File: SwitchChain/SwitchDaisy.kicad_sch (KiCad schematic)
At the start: 2 parts, among them SW101 SW_Push

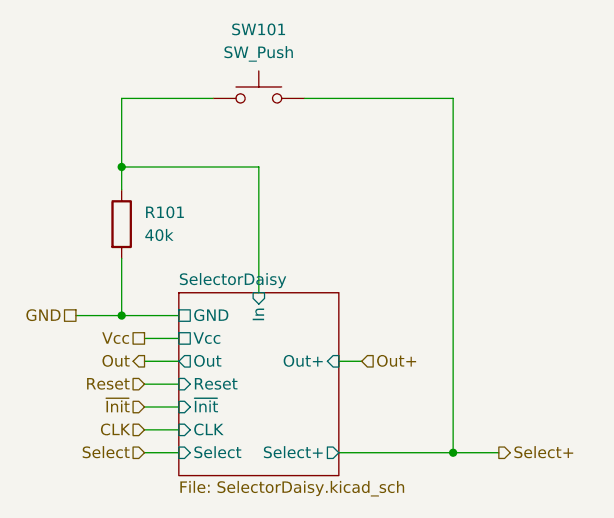
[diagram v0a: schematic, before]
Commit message: fix pin label, reduce column keys to 4
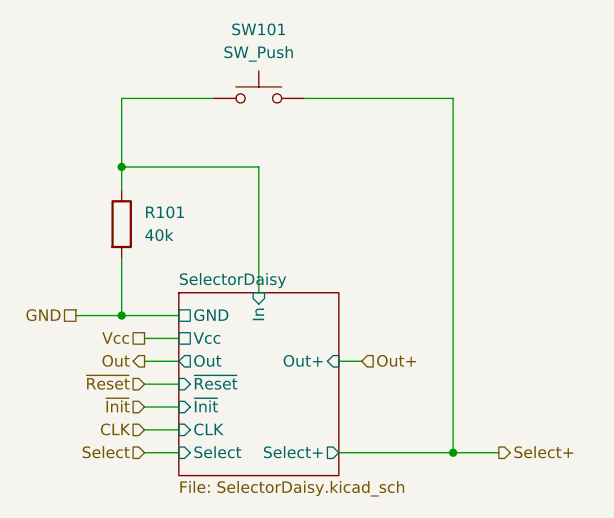
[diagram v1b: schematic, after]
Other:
- sheet SelectorDaisy ports: added ~{Reset}; removed Reset
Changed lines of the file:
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@@
 		)
 	)
-	(hierarchical_label "Reset"
+	(hierarchical_label "~{Reset}"
 		(shape input)
 		(at 115.57 129.54 180)
@@
 				(path "/bdfc27f9-2f87-4fe7-a85f-b21fa09d30f0/1ab69dab-5bac-40ee-8e89-7d9f544d3dd1"
 					(reference "R301")
-					(unit 1)
-				)
-				(path "/bdfc27f9-2f87-4fe7-a85f-b21fa09d30f0/253992b3-02ab-4aad-9a1e-d76b1438e691"
-					(reference "R1001")
 					(unit 1)
 				)
@@
 					(unit 1)
 				)
-				(path "/bdfc27f9-2f87-4fe7-a85f-b21fa09d30f0/253992b3-02ab-4aad-9a1e-d76b1438e691"
-					(reference "SW1001")
-					(unit 1)
-				)
 				(path "/bdfc27f9-2f87-4fe7-a85f-b21fa09d30f0/95715d47-4288-4034-bf4d-8592fbea460b"
 					(reference "SW501")
@@
 			)
 		)
-		(pin "Reset" input
-			(at 119.38 129.54 180)
-			(effects
-				(font
-					(size 1.27 1.27)
-				)
-				(justify left)
-			)
-		)
 		(pin "CLK" input
 			(at 119.38 134.62 180)
@@
 				)
 				(justify right)
+			)
+		)
+		(pin "~{Reset}" input
+			(at 119.38 129.54 180)
+			(effects
+				(font
+					(size 1.27 1.27)
+				)
+				(justify left)
 			)
 		)
@@
 					(page "9")
 				)
-				(path "/bdfc27f9-2f87-4fe7-a85f-b21fa09d30f0/253992b3-02ab-4aad-9a1e-d76b1438e691"
-					(page "11")
-				)
 			)
 			(project "SwitchDaisy"
@@
 		)
 	)
-	(sheet_instances
-		(path "/"
-			(page "1")
-		)
-	)

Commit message: change connector
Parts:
- R101: Manufacturer Part number (none) -> RNCF0402BTE40K0; Original (none) -> N; Purchase Link (none) -> https://www.digikey.com/en/products/detail/stackpole-electr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
- SW101: Manufacturer Part number (none) -> 5118; Original (none) -> Y; Purchase Link (none) -> https://www.digikey.com/en/products/detail/adafruit-industr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
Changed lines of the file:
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@@
 			)
 		)
-		(property "Description" "Resistor"
+		(property "Description" "RES SMD 40K OHM 0.1% 1/10W 0402"
+			(at 113.03 111.76 0)
+			(effects
+				(font
+					(size 1.27 1.27)
+				)
+				(hide yes)
+			)
+		)
+		(property "Manufacturer Part number" "RNCF0402BTE40K0"
+			(at 113.03 111.76 0)
+			(effects
+				(font
+					(size 1.27 1.27)
+				)
+				(hide yes)
+			)
+		)
+		(property "Original" "N"
+			(at 113.03 111.76 0)
+			(effects
+				(font
+					(size 1.27 1.27)
+				)
+				(hide yes)
+			)
+		)
+		(property "Purchase Link" "https://www.digikey.com/en/products/detail/stackpole-electronics-inc/RNCF0402BTE40K0/6259278"
 			(at 113.03 111.76 0)
 			(effects
@@
 			)
 		)
-		(property "Description" "Push button switch, generic, two pins"
+		(property "Description" "SWITCH SKT FOR KAILH CHOC 1=10PC"
 			(at 128.27 97.79 0)
 			(effects
+				(font
+					(size 1.27 1.27)
+				)
+				(hide yes)
+			)
+		)
+		(property "Manufacturer Part number" "5118"
+			(at 128.27 97.79 0)
+			(effects
+				(font
+					(size 1.27 1.27)
+				)
+				(hide yes)
+			)
+		)
+		(property "Original" "Y"
+			(at 128.27 97.79 0)
+			(effects
+				(font
+					(size 1.27 1.27)
+				)
+				(hide yes)
+			)
+		)
+		(property "Purchase Link" "https://www.digikey.com/en/products/detail/adafruit-industries-llc/5118/14671678"
+			(at 128.27 97.79 0)
+			(effects
